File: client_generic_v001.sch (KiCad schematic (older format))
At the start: 10 parts, among them P1 CONN_01X06, P2 CONN_01X08, SW1 DIPS_08, SW2 SW_PUSH, SW3 SW_PUSH, U1 ESP-12_Breakout, U2 MCP23017, U3 MCP3208, U4 WS2812B

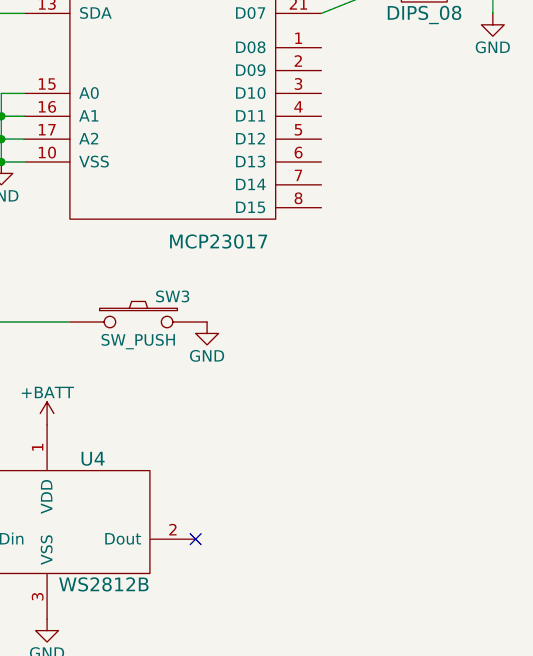
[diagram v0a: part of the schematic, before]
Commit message: Added status LEDs
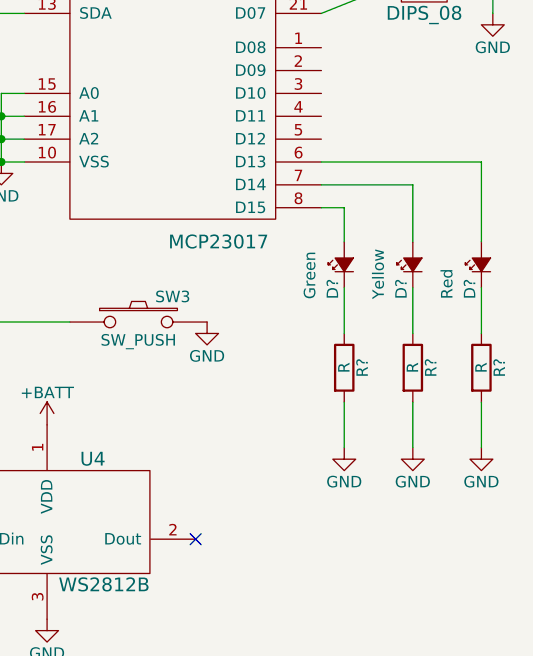
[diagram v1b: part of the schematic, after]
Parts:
- added D?: Yellow, symbol Led_Small
- added D?: Green, symbol Led_Small
- added D?: Red, symbol Led_Small
- added R? (x3): R, symbol R
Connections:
- net GND: now also R?.2, R?.2, R?.2
- net at U2.6 (D13): now also D?.2 (A)
- net at U2.7 (D14): now also D?.2 (A)
- net at U2.8 (D15): now also D?.2 (A)
- new net: D?.1 (K), R?.1 (x3)
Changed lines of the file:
@@
 	0    1    1    0
 $EndComp
-Connection ~ 3100 2350
-Wire Wire Line
-	3000 2500 3000 2350
-Wire Wire Line
-	3000 2350 3200 2350
-Wire Wire Line
-	3200 2350 3200 2500
-Connection ~ 3100 3800
-Connection ~ 6700 3450
-Connection ~ 6700 3550
-Wire Wire Line
-	6700 3450 6800 3450
-Wire Wire Line
-	6700 3250 6700 3550
-Wire Wire Line
-	6700 3550 6800 3550
-Connection ~ 6800 2350
-Wire Wire Line
-	6800 2000 6800 2450
-Wire Wire Line
-	3800 3000 4300 3000
-Wire Wire Line
-	3800 3100 4300 3100
-Wire Wire Line
-	3800 3200 4300 3200
-Wire Wire Line
-	4350 4100 6300 4100
-Wire Wire Line
-	6300 4100 6300 3200
-Wire Wire Line
-	3800 3300 4350 3300
-Wire Wire Line
-	4350 3300 4350 4100
-Wire Wire Line
-	5400 1800 5400 2000
-Wire Wire Line
-	6300 2800 6800 2800
-Wire Wire Line
-	6300 2900 6800 2900
-Wire Wire Line
-	6300 1800 6300 2600
-Wire Wire Line
-	6300 2700 6400 2700
-Wire Wire Line
-	6400 2700 6400 2200
-Wire Wire Line
-	6400 2200 6200 2200
-Wire Wire Line
-	6200 2200 6200 1800
-Connection ~ 5400 2000
-Wire Wire Line
-	6100 1800 6100 2000
-Wire Wire Line
-	6100 2000 5400 2000
-Wire Wire Line
-	6700 3350 6800 3350
-Wire Wire Line
-	4300 2250 4300 2600
-Wire Wire Line
-	6300 3000 6500 3000
-Wire Wire Line
-	6500 3000 6500 4250
-Wire Wire Line
-	6500 4250 7000 4250
-Wire Wire Line
-	6300 3100 6400 3100
-Wire Wire Line
-	6400 5200 6450 5200
-Wire Wire Line
-	6400 5200 6400 4950
-Wire Wire Line
-	6400 3100 6400 4650
-Wire Wire Line
-	8100 2200 8350 2100
-Wire Wire Line
-	8100 2300 8350 2200
-Wire Wire Line
-	8100 2400 8350 2300
-Wire Wire Line
-	8100 2500 8350 2400
-Wire Wire Line
-	8100 2600 8350 2500
-Wire Wire Line
-	8100 2700 8350 2600
-Wire Wire Line
-	8100 2800 8350 2700
-Wire Wire Line
-	8100 2900 8350 2800
 $Comp
 L MCP23017 U2
@@
 	1    0    0    -1
 $EndComp
-Wire Wire Line
-	3000 3800 3200 3800
 $Comp
 L +BATT #PWR011
@@
 	1    0    0    -1
 $EndComp
-Wire Wire Line
-	8750 2100 8850 2100
-Wire Wire Line
-	8850 2100 8850 2900
 $Comp
 L GND #PWR012
@@
 	1    0    0    -1
 $EndComp
-Wire Wire Line
-	8750 2200 8850 2200
-Connection ~ 8850 2200
-Wire Wire Line
-	8750 2300 8850 2300
-Connection ~ 8850 2300
-Wire Wire Line
-	8750 2400 8850 2400
-Connection ~ 8850 2400
-Wire Wire Line
-	8750 2500 8850 2500
-Connection ~ 8850 2500
-Wire Wire Line
-	8750 2600 8850 2600
-Connection ~ 8850 2600
-Wire Wire Line
-	8750 2700 8850 2700
-Connection ~ 8850 2700
-Wire Wire Line
-	8850 2800 8750 2800
-Connection ~ 8850 2800
-Wire Wire Line
-	6800 3250 6700 3250
-Connection ~ 6700 3350
 $Comp
 L +BATT #PWR013
@@
 Text GLabel 2200 5300 0    60   Input ~ 0
 BattSense
+NoConn ~ 2600 5300
+$Comp
+L Led_Small D?
+U 1 1 577EFCCF
+P 8500 4000
+F 0 "D?" H 8350 4050 50  0000 L CNN
+F 1 "Yellow" H 8350 4150 50  0000 L CNN
+F 2 "" V 8500 4000 50  0000 C CNN
+F 3 "" V 8500 4000 50  0000 C CNN
+	1    8500 4000
+	0    -1   -1   0
+$EndComp
+$Comp
+L Led_Small D?
+U 1 1 577EFD55
+P 8200 4000
+F 0 "D?" H 8050 4050 50  0000 L CNN
+F 1 "Green" H 8050 4150 50  0000 L CNN
+F 2 "" V 8200 4000 50  0000 C CNN
+F 3 "" V 8200 4000 50  0000 C CNN
+	1    8200 4000
+	0    -1   -1   0
+$EndComp
+Connection ~ 3100 2350
+Wire Wire Line
+	3000 2500 3000 2350
+Wire Wire Line
+	3000 2350 3200 2350
+Wire Wire Line
+	3200 2350 3200 2500
+Connection ~ 3100 3800
+Connection ~ 6700 3450
+Connection ~ 6700 3550
+Wire Wire Line
+	6700 3450 6800 3450
+Wire Wire Line
+	6700 3250 6700 3550
+Wire Wire Line
+	6700 3550 6800 3550
+Connection ~ 6800 2350
+Wire Wire Line
+	6800 2000 6800 2450
+Wire Wire Line
+	3800 3000 4300 3000
+Wire Wire Line
+	3800 3100 4300 3100
+Wire Wire Line
+	3800 3200 4300 3200
+Wire Wire Line
+	4350 4100 6300 4100
+Wire Wire Line
+	6300 4100 6300 3200
+Wire Wire Line
+	3800 3300 4350 3300
+Wire Wire Line
+	4350 3300 4350 4100
+Wire Wire Line
+	5400 1800 5400 2000
+Wire Wire Line
+	6300 2800 6800 2800
+Wire Wire Line
+	6300 2900 6800 2900
+Wire Wire Line
+	6300 1800 6300 2600
+Wire Wire Line
+	6300 2700 6400 2700
+Wire Wire Line
+	6400 2700 6400 2200
+Wire Wire Line
+	6400 2200 6200 2200
+Wire Wire Line
+	6200 2200 6200 1800
+Connection ~ 5400 2000
+Wire Wire Line
+	6100 1800 6100 2000
+Wire Wire Line
+	6100 2000 5400 2000
+Wire Wire Line
+	6700 3350 6800 3350
+Wire Wire Line
+	4300 2250 4300 2600
+Wire Wire Line
+	6300 3000 6500 3000
+Wire Wire Line
+	6500 3000 6500 4250
+Wire Wire Line
+	6500 4250 7000 4250
+Wire Wire Line
+	6300 3100 6400 3100
+Wire Wire Line
+	6400 5200 6450 5200
+Wire Wire Line
+	6400 5200 6400 4950
+Wire Wire Line
+	6400 3100 6400 4650
+Wire Wire Line
+	8100 2200 8350 2100
+Wire Wire Line
+	8100 2300 8350 2200
+Wire Wire Line
+	8100 2400 8350 2300
+Wire Wire Line
+	8100 2500 8350 2400
+Wire Wire Line
+	8100 2600 8350 2500
+Wire Wire Line
+	8100 2700 8350 2600
+Wire Wire Line
+	8100 2800 8350 2700
+Wire Wire Line
+	8100 2900 8350 2800
+Wire Wire Line
+	3000 3800 3200 3800
+Wire Wire Line
+	8750 2100 8850 2100
+Wire Wire Line
+	8850 2100 8850 2900
+Wire Wire Line
+	8750 2200 8850 2200
+Connection ~ 8850 2200
+Wire Wire Line
+	8750 2300 8850 2300
+Connection ~ 8850 2300
+Wire Wire Line
+	8750 2400 8850 2400
+Connection ~ 8850 2400
+Wire Wire Line
+	8750 2500 8850 2500
+Connection ~ 8850 2500
+Wire Wire Line
+	8750 2600 8850 2600
+Connection ~ 8850 2600
+Wire Wire Line
+	8750 2700 8850 2700
+Connection ~ 8850 2700
+Wire Wire Line
+	8850 2800 8750 2800
+Connection ~ 8850 2800
+Wire Wire Line
+	6800 3250 6700 3250
+Connection ~ 6700 3350
 Wire Wire Line
 	2200 5300 2600 5300
-NoConn ~ 2600 5300
+$Comp
+L R R?
+U 1 1 577F01E7
+P 8500 4450
+F 0 "R?" V 8580 4450 50  0000 C CNN
+F 1 "R" V 8500 4450 50  0000 C CNN
+F 2 "" V 8430 4450 50  0000 C CNN
+F 3 "" H 8500 4450 50  0000 C CNN
+	1    8500 4450
+	1    0    0    -1
+$EndComp
+$Comp
+L R R?
+U 1 1 577F0283
+P 8200 4450
+F 0 "R?" V 8280 4450 50  0000 C CNN
+F 1 "R" V 8200 4450 50  0000 C CNN
+F 2 "" V 8130 4450 50  0000 C CNN
+F 3 "" H 8200 4450 50  0000 C CNN
+	1    8200 4450
+	1    0    0    -1
+$EndComp
+$Comp
+L Led_Small D?
+U 1 1 577F09E1
+P 8800 4000
+F 0 "D?" H 8650 4050 50  0000 L CNN
+F 1 "Red" H 8650 4150 50  0000 L CNN
+F 2 "" V 8800 4000 50  0000 C CNN
+F 3 "" V 8800 4000 50  0000 C CNN
+	1    8800 4000
+	0    -1   -1   0
+$EndComp
+$Comp
+L R R?
+U 1 1 577F0B28
+P 8800 4450
+F 0 "R?" V 8880 4450 50  0000 C CNN
+F 1 "R" V 8800 4450 50  0000 C CNN
+F 2 "" V 8730 4450 50  0000 C CNN
+F 3 "" H 8800 4450 50  0000 C CNN
+	1    8800 4450
+	1    0    0    -1
+$EndComp
+Wire Wire Line
+	8200 4100 8200 4300
+Wire Wire Line
+	8500 4100 8500 4300
+Wire Wire Line
+	8800 4100 8800 4300
+$Comp
+L GND #PWR?
+U 1 1 577F0CAD
+P 8200 4800
+F 0 "#PWR?" H 8200 4550 50  0001 C CNN
+F 1 "GND" H 8200 4650 50  0000 C CNN
+F 2 "" H 8200 4800 50  0000 C CNN
+F 3 "" H 8200 4800 50  0000 C CNN
+	1    8200 4800
+	1    0    0    -1
+$EndComp
+$Comp
+L GND #PWR?
+U 1 1 577F0CFF
+P 8500 4800
+F 0 "#PWR?" H 8500 4550 50  0001 C CNN
+F 1 "GND" H 8500 4650 50  0000 C CNN
+F 2 "" H 8500 4800 50  0000 C CNN
+F 3 "" H 8500 4800 50  0000 C CNN
+	1    8500 4800
+	1    0    0    -1
+$EndComp
+$Comp
+L GND #PWR?
+U 1 1 577F0D3A
+P 8800 4800
+F 0 "#PWR?" H 8800 4550 50  0001 C CNN
+F 1 "GND" H 8800 4650 50  0000 C CNN
+F 2 "" H 8800 4800 50  0000 C CNN
+F 3 "" H 8800 4800 50  0000 C CNN
+	1    8800 4800
+	1    0    0    -1
+$EndComp
+Wire Wire Line
+	8200 4600 8200 4800
+Wire Wire Line
+	8500 4600 8500 4800
+Wire Wire Line
+	8800 4600 8800 4800
+Wire Wire Line
+	8100 3750 8200 3750
+Wire Wire Line
+	8200 3750 8200 3900
+Wire Wire Line
+	8100 3650 8500 3650
+Wire Wire Line
+	8500 3650 8500 3900
+Wire Wire Line
+	8100 3550 8800 3550
+Wire Wire Line
+	8800 3550 8800 3900
 $EndSCHEMATC
